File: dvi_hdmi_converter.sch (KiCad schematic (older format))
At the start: 3 parts, among them J0 HDMI_A, J1 HDMI_A, J2 DVI-DP-29-C-G-HN-4

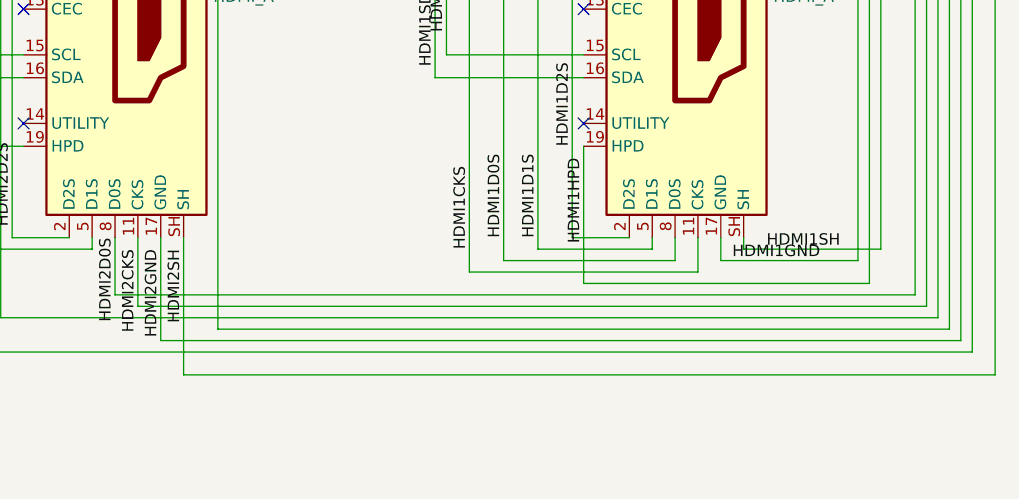
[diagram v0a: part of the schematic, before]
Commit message: traced out first hdmi port
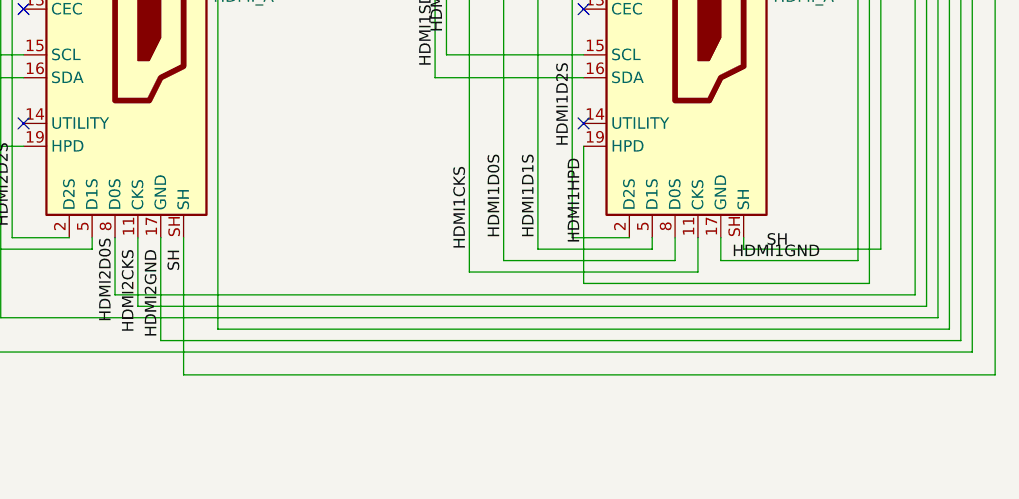
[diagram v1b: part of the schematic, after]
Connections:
- net HDMI2SH is gone; now on net SH: J1.SH, J2.SH2
- net HDMI1SH renamed SH
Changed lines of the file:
@@
 HDMI2GND
 Text Label 2950 6650 3    50   ~ 0
-HDMI2SH
+SH
 Text Label 5150 4050 0    50   ~ 0
 HDMI15V
@@
 HDMI1GND
 Text Label 5500 6650 0    50   ~ 0
-HDMI1SH
+SH
 $EndSCHEMATC

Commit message: latest update with schematic
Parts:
- J2: footprint footprints:DVI-DP-29-C-G-HN-4 -> footprints:DVI-DP-29-C-G-HN-4-no-analog
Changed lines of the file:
@@
 F 0 "J2" H 7500 3700 50  0000 R CNN
 F 1 "DVI-DP-29-C-G-HN-4" H 7900 3800 50  0000 R CNN
-F 2 "footprints:DVI-DP-29-C-G-HN-4" H 7550 3800 50  0001 C CNN
+F 2 "footprints:DVI-DP-29-C-G-HN-4-no-analog" H 7550 3800 50  0001 C CNN
 F 3 "" H 7550 3800 50  0001 C CNN
 	1    7550 3800
